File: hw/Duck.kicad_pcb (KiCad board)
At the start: 2 copper layers, 35.3 x 20.8 mm, 32 parts, among them J1 Conn_01x06, J2 Conn_01x04, J3 USB_C_Receptacle_USB2.0_14P, J4 Conn_01x06, Q1 MMBT3904, Q2 MMBT3904, U1 ESP32-S3-MINI-1, U2 SPX3819M5-L-3-3, U3 INMP441, U4 MAX17048G+T10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

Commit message: hw: Routing
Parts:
- JP1: moved to F.Cu
- moved JP1 2.15 mm to (83.2, 53.8)
- moved C3 0.72 mm to (64.8, 51.9), turned to 90 degrees
- moved C7 0.20 mm to (80.1, 53.0)
- moved C8 0.20 mm to (81.0, 53.0)
- moved C9 0.20 mm to (83.9, 50.4)
- moved J3 0.20 mm to (89.8, 49.5)
- moved Q1 0.20 mm to (81.5, 45.7)
- moved R6 0.20 mm to (84.3, 47.1)
- moved R7 0.20 mm to (83.9, 51.3)
- moved R8 0.20 mm to (83.7, 43.9)
- moved R9 0.20 mm to (79.3, 46.4)
- moved U5 0.20 mm to (80.9, 50.0)
- moved J2 0.20 mm to (57.8, 43.7)
- moved J4 0.20 mm to (77.0, 53.7)
- moved Q2 0.20 mm to (81.5, 41.8)
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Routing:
- net +3V3: track 0.00 -> 41.0 mm, vias 0 -> 2
- net +BATT: track 0.00 -> 37.9 mm, vias 0 -> 1
- net /BOOT0: track 0.00 -> 32.1 mm, vias 0 -> 2
- net VBUS: track 0.00 -> 18.9 mm
- net /ESP_EN: track 0.00 -> 17.8 mm, vias 0 -> 1
- net /U0TXD: track 0.00 -> 17.0 mm, vias 0 -> 1
- net /U0RXD: track 0.00 -> 14.4 mm, vias 0 -> 1
- net /DTR: track 0.00 -> 9.76 mm
- net /REG_OUT: track 0.00 -> 8.16 mm, vias 0 -> 2
- net /USB_D-: track 0.00 -> 6.97 mm, vias 0 -> 2
- net /RTS: track 0.00 -> 6.32 mm
- net /SDA: track 0.00 -> 5.77 mm, vias 0 -> 1
- net /SCL: track 0.00 -> 5.63 mm, vias 0 -> 1
- net /USB_D+: track 0.00 -> 5.14 mm
- net /MIC_EN: track 0.00 -> 5.05 mm
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- added copper zone on B.Cu, net +3V3
- added copper zone on F.Cu, net /USB_D+
- added copper zone on B.Cu, net GND
- added copper zone on F.Cu, net GND
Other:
- board size 35.3 x 20.8 mm -> 35.5 x 20.8 mm

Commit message: hw: Minor revisions
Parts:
- added G***: LOGO, LOGO, F.Cu at (71.7, 56.9)
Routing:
- net GND: track 0.00 -> 2.13 mm
- net +BATT: vias 1 -> 2
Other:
- outline, holes or cut-outs redrawn
- board text added: "<24-Flurry"
- board text added: ">"
- board text added: "Rev. 1"

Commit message: hw: Finalize (...or is it?)
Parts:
- added G***: LOGO, LOGO, B.Cu at (80.7, 41.6)
- moved G*** 0.20 mm to (71.7, 56.7)
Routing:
- net +BATT: track 37.9 -> 37.3 mm
- net GND: vias 148 -> 150
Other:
- outline, holes or cut-outs redrawn
- board text added: "Round Tracks → Teardrops → Refill & DRC"

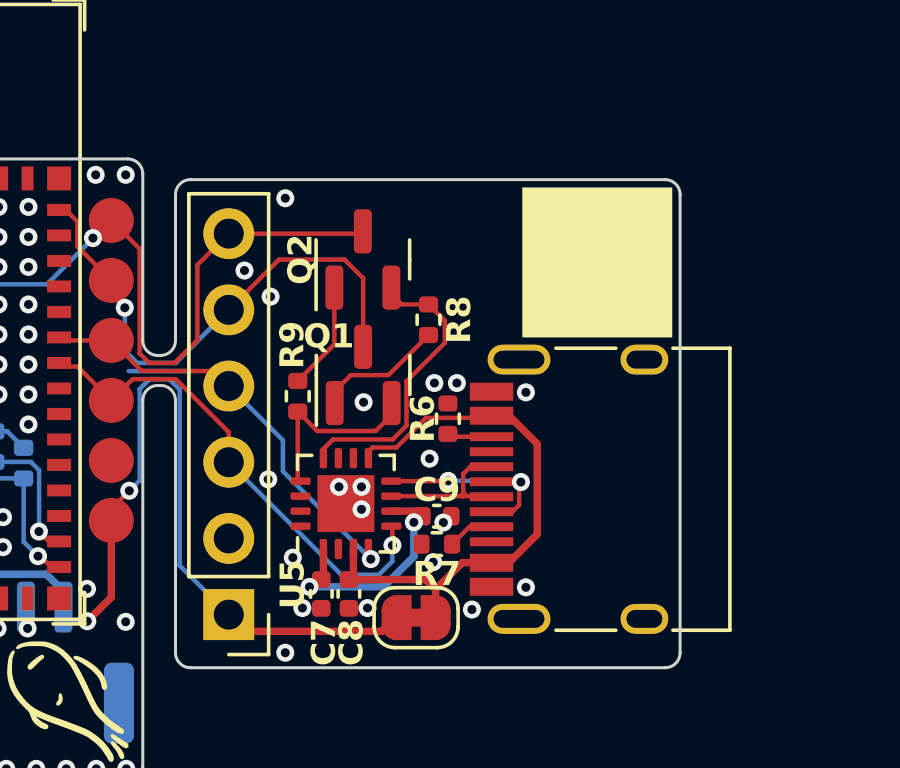
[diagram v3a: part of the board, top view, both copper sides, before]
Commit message: hw: Finalize; submit for fab (Rev. 1)
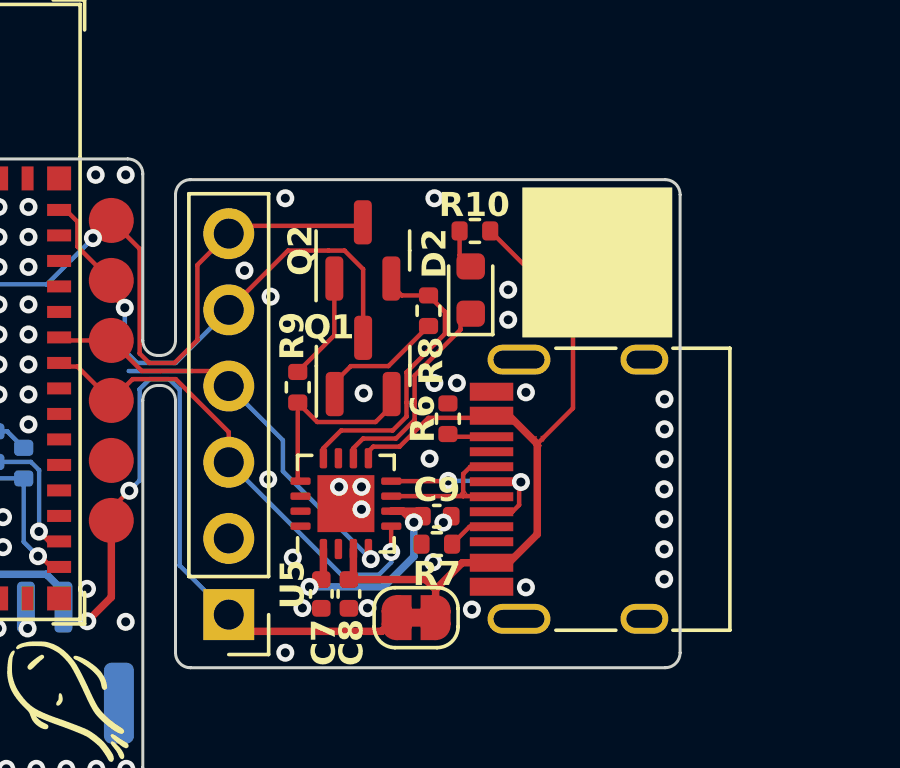
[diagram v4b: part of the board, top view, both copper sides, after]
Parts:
- added D2: White, LED_SMD:LED_0603_1608Metric, F.Cu at (85.1, 42.9)
- added R10: 10k, Resistor_SMD:R_0402_1005Metric, F.Cu at (85.2, 40.9)
- moved Q2 0.30 mm to (81.5, 41.5)
- moved R8 0.30 mm to (83.7, 43.5)
- moved Q1 0.30 mm to (81.5, 45.4)
- moved R9 0.30 mm to (79.3, 46.1)
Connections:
- U5 pad 10: unconnected-(U5-ACT#-Pad10) -> /ACT
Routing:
- net VBUS: track 18.9 -> 27.7 mm
- net /ACT: track 0.00 -> 6.88 mm
- net Net-(D2-A): track 0.00 -> 1.34 mm
- net /REG_OUT: track 8.06 -> 8.97 mm
- net GND: vias 150 -> 160
- added copper zone on F.Cu, net VBUS
